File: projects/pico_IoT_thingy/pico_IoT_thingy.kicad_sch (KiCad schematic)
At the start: 2 parts, among them U1 TSR1-2450E

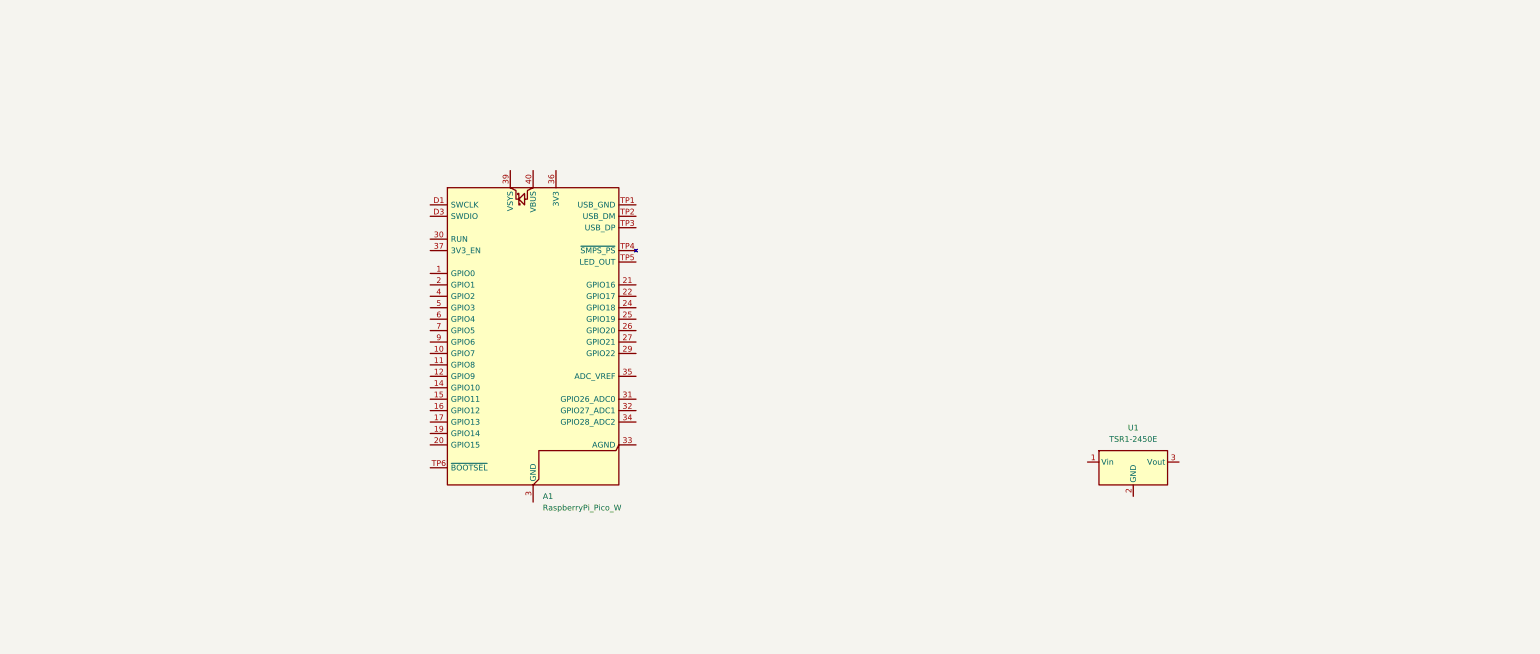
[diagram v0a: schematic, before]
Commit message: Pico IoT thingy - Add 5V to 3V3 bar
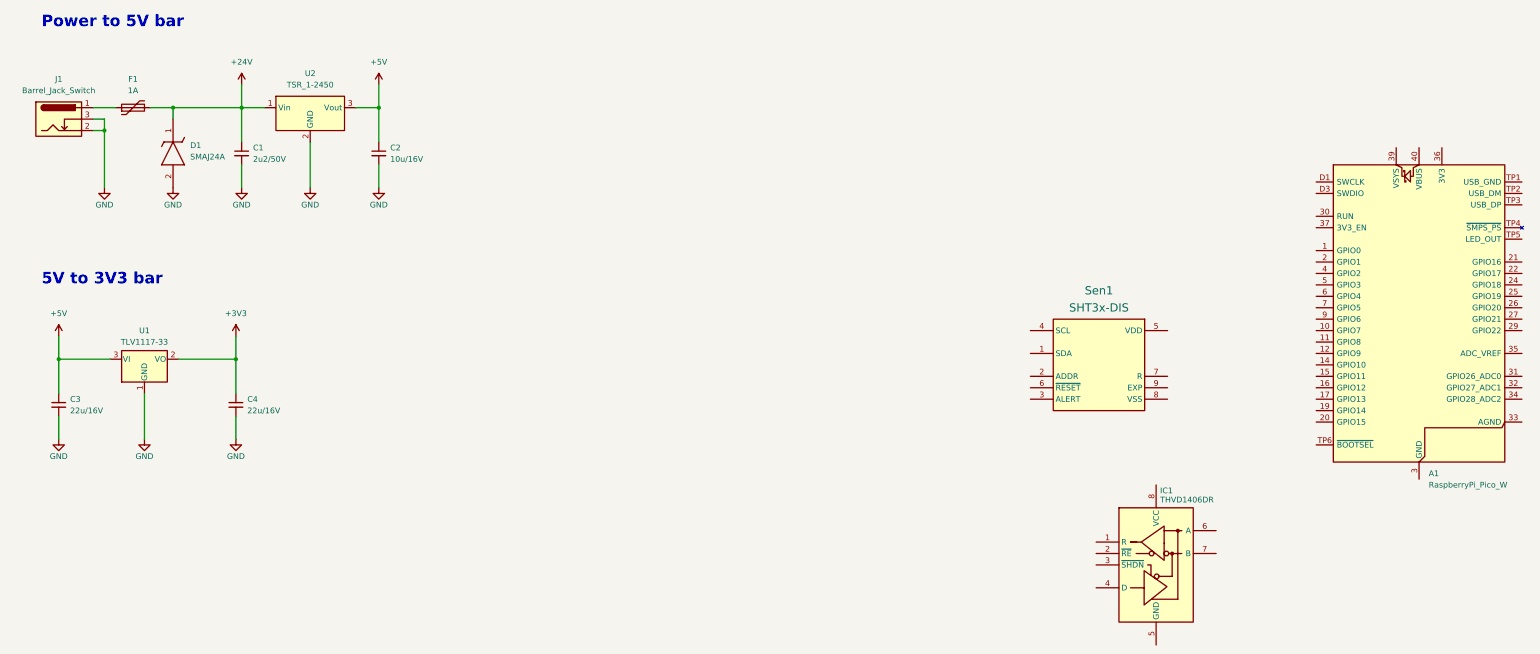
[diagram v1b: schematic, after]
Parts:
- removed U1: TSR1-2450E, Converter_DCDC:Converter_DCDC_TRACO_TSR1-xxxxE_THT, symbol Converter_DCDC:TSR1-2450E
- added C1: 2u2/50V, symbol Device:C_Small
- added C2: 10u/16V, symbol Device:C_Small
- added C3, C4: 22u/16V, symbol Device:C_Small
- added D1: SMAJ24A, DIOM5127X229N, symbol MH_SMAJ24A:SMAJ24A
- added F1: 1A, symbol Device:Polyfuse
- added IC1: THVD1406DR, SOIC127P600X175-8N, symbol MH_THVD1406DR:THVD1406DR
- added J1: Barrel_Jack_Switch, symbol Connector:Barrel_Jack_Switch
- added Sen1: SHT3x-DIS, symbol MH_SHT31-DIS:SHT3x-DIS
- added U1: TLV1117-33, symbol Regulator_Linear:TLV1117-33
- added U2: TSR_1-2450, Converter_DCDC:Converter_DCDC_TRACO_TSR-1_THT, symbol Converter_DCDC:TSR_1-2450
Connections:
- new net: F1.1, J1.1
- new net +24V: C1.1, D1.1 (K), F1.2, U2.1 (Vin)
- new net +3V3: C4.1, U1.2 (VO)
- new net +5V: C2.1, C3.1, U1.3 (VI), U2.3 (Vout)
- new net GND: C1.2, C2.2, C3.2, C4.2, D1.2 (A), J1.2, J1.3, U1.1 (GND), U2.2 (GND)
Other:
- note added: "5V to 3V3 bar"
- note added: "Power to 5V bar"
- moved on the sheet: A1

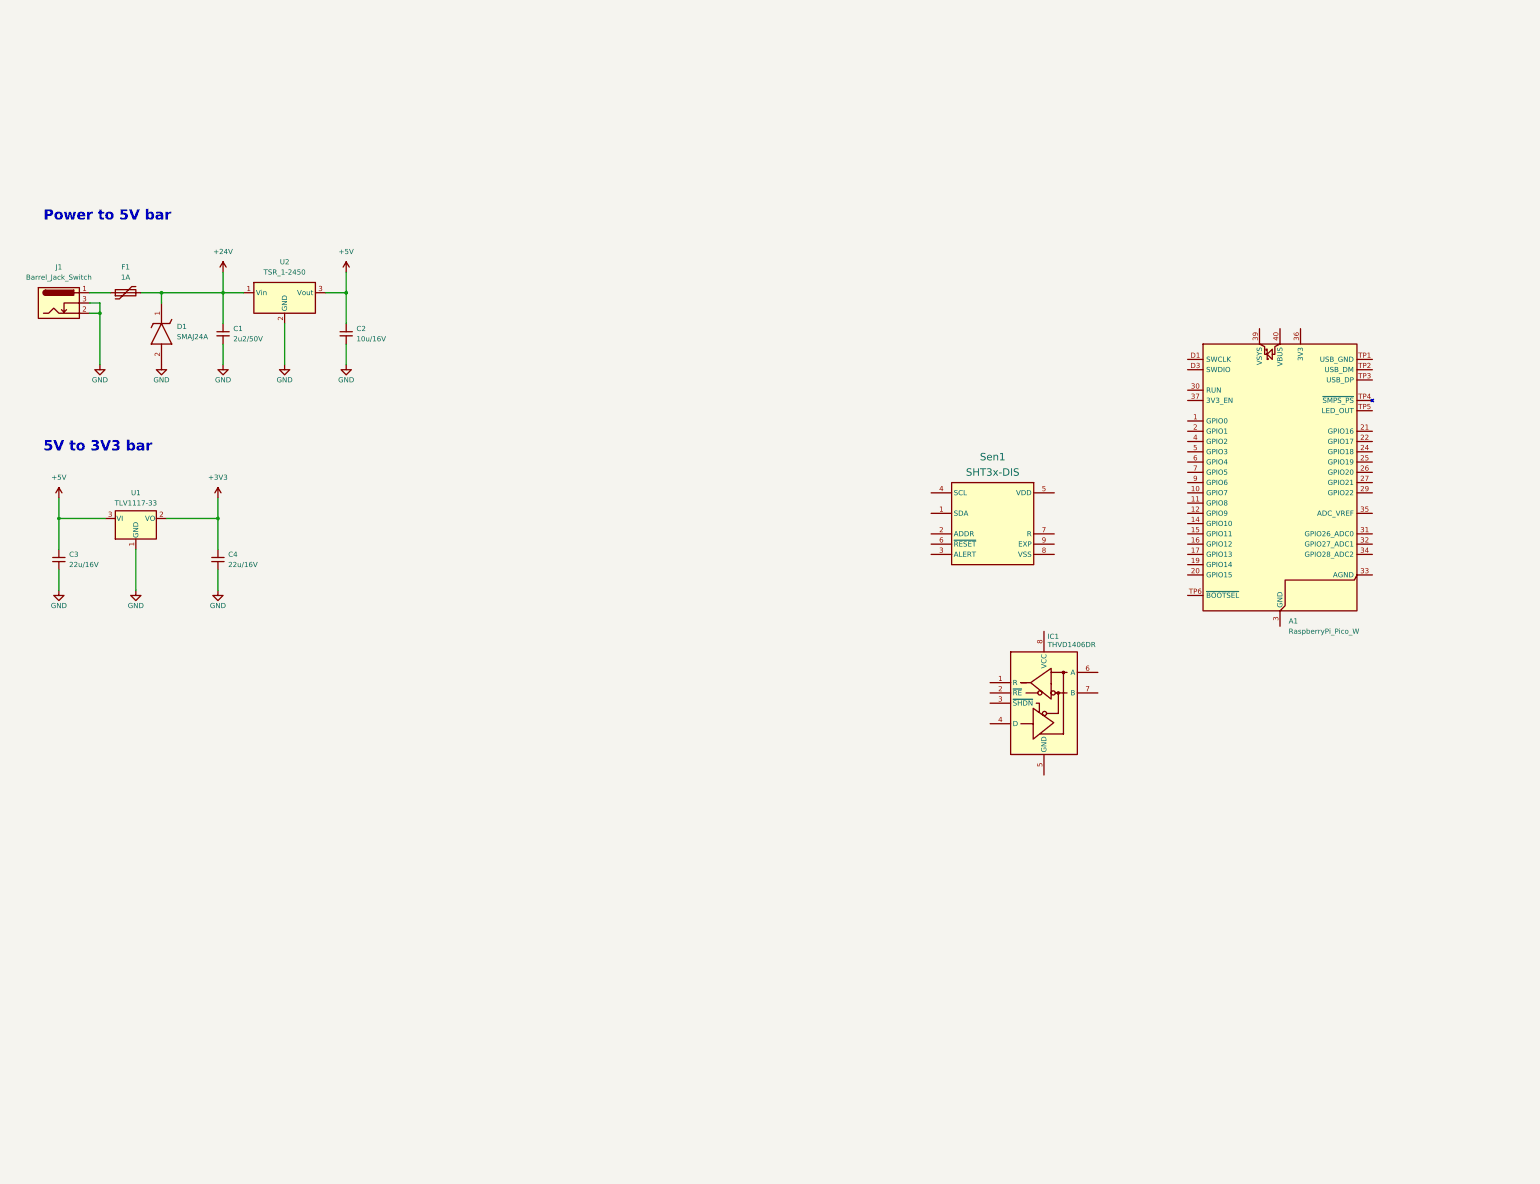
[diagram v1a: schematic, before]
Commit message: Pico IoT thingy - progress on schematics
- user-programmable button
- RGB LED
- DIP switch to set address
- SPI port
- SHT31 sensor
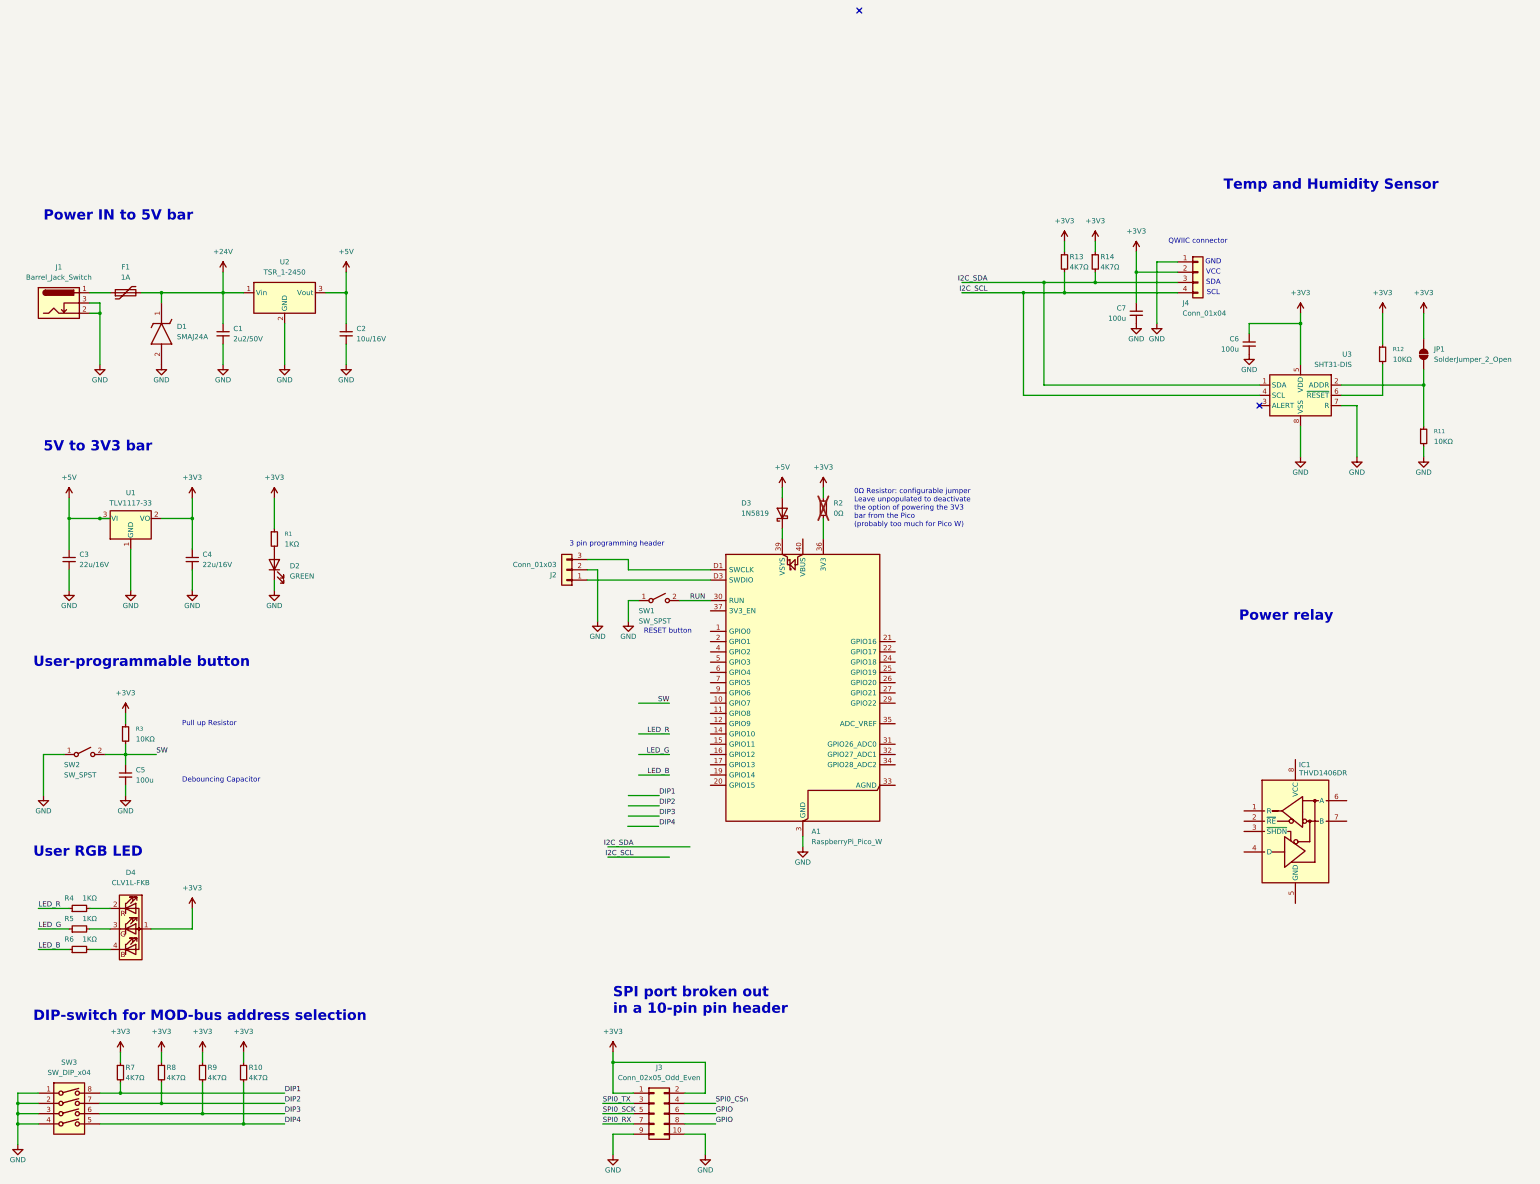
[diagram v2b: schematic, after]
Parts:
- removed A1: RaspberryPi_Pico_W, Module:RaspberryPi_Pico_W_SMD, symbol MCU_Module:RaspberryPi_Pico_W_Extensive
- removed Sen1: SHT3x-DIS, symbol MH_SHT31-DIS:SHT3x-DIS
- added A1: RaspberryPi_Pico_W, Module:RaspberryPi_Pico_W_SMD_HandSolder, symbol MCU_Module:RaspberryPi_Pico_W_Debug
- added C5, C6, C7: 100u, symbol Device:C_Small
- added D2: GREEN, symbol Device:LED
- added D3: 1N5819, Diode_THT:D_DO-41_SOD81_P10.16mm_Horizontal, symbol Diode:1N5819
- added D4: CLV1L-FKB, LED_SMD:LED_Cree-PLCC4_3.2x2.8mm_CCW, symbol LED:CLV1L-FKB
- added J2: Conn_01x03, symbol Connector_Generic:Conn_01x03
- added J3: Conn_02x05_Odd_Even, symbol Connector_Generic:Conn_02x05_Odd_Even
- added J4: Conn_01x04, symbol Connector_Generic:Conn_01x04
- added JP1: SolderJumper_2_Open, symbol Jumper:SolderJumper_2_Open
- added R1, R4, R5, R6: 1KΩ, symbol Device:R_Small
- added R10, R13, R14, R7, R8, R9: 4K7Ω, symbol Device:R_Small
- added R11, R12, R3: 10KΩ, symbol Device:R_Small
- added R2: 0Ω, symbol Device:R_Small
- added SW1, SW2: SW_SPST, symbol Switch:SW_SPST
- added SW3: SW_DIP_x04, symbol Switch:SW_DIP_x04
- added U3: SHT31-DIS, Sensor_Humidity:Sensirion_DFN-8-1EP_2.5x2.5mm_P0.5mm_EP1.1x1.7mm, symbol Sensor_Humidity:SHT31-DIS
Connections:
- net +3V3: now also C6.1, C7.1, D4.1 (A), J3.1 (Pin_1), J3.2 (Pin_2), J4.2 (Pin_2), JP1.2 (B), R1.1, R10.1, R12.1, R13.1, R14.1, R2.1, R3.1, R7.1, R8.1, R9.1, U3.5 (VDD)
- net +5V: now also D3.2 (A)
- net GND: now also A1.13 (GND), A1.18 (GND), A1.23 (GND), A1.28 (GND), A1.3 (GND), A1.38 (GND), A1.8 (GND), A1.D2 (GND), C5.2, C6.2, C7.2, D2.1 (K), J2.2 (Pin_2), J3.10 (Pin_10), J3.9 (Pin_9), J4.1 (Pin_1), R11.2, SW1.1 (A), SW2.1 (A), SW3.1, SW3.2, SW3.3, SW3.4, U3.7 (R), U3.8 (VSS), U3.9 (VSS)
- new net: R12.2, U3.6 (~{RESET})
- new net: A1.D3 (SWDIO), J2.1 (Pin_1)
- new net: A1.D1 (SWCLK), J2.3 (Pin_3)
- new net: A1.36 (3V3), R2.2
- new net: A1.39 (VSYS), D3.1 (K)
- new net: D4.2 (RK), R4.2
- new net: D4.3 (GK), R5.2
- new net: D4.4 (BK), R6.2
- new net: JP1.1 (A), R11.1, U3.2 (ADDR)
- new net: D2.2 (A), R1.2
- new net DIP1: R7.2, SW3.8
- new net DIP2: R8.2, SW3.7
- new net DIP3: R9.2, SW3.6
- new net DIP4: R10.2, SW3.5
- new net GPIO: J3.6 (Pin_6), J3.8 (Pin_8)
- new net I2C_SCL: J4.4 (Pin_4), R13.2, U3.4 (SCL)
- new net I2C_SDA: J4.3 (Pin_3), R14.2, U3.1 (SDA)
- new net LED_B: R6.1
- new net LED_G: R5.1
- new net LED_R: R4.1
- new net RUN: A1.30 (RUN), SW1.2 (B)
- new net SPI0_CSn: J3.4 (Pin_4)
- new net SPI0_RX: J3.7 (Pin_7)
- new net SPI0_SCK: J3.5 (Pin_5)
- new net SPI0_TX: J3.3 (Pin_3)
- new net SW: C5.1, R3.2, SW2.2 (B)
- no-connect marks 0 -> 2
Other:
- note added: "0Ω Resistor: configurable jumper Leave unpopulated to deactivate the option of powering the 3V3 bar from the Pico (probably too much for Pico W)"
- note added: "3 pin programming header"
- note added: "DIP-switch for MOD-bus address selection"
- note added: "Debouncing Capacitor"
- note added: "GND"
- note added: "Power IN to 5V bar"
- note added: "Power relay"
- note added: "Pull up Resistor"
- note added: "QWIIC connector"
- note added: "RESET button"
- note added: "SCL"
- note added: "SDA"
- note added: "SPI port broken out in a 10-pin pin header"
- note added: "Temp and Humidity Sensor"
- note added: "User RGB LED"
- note added: "User-programmable button"
- note added: "VCC"
- note removed: "Power to 5V bar"
- moved on the sheet: C3, C4, IC1, U1

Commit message: Pico IoT thingy - complete schematics, DRC OK
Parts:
- removed D3: 1N5819, Diode_THT:D_DO-41_SOD81_P10.16mm_Horizontal, symbol Diode:1N5819
- added C8: 100n, symbol Device:C_Small
- added D3: SM712_SOT23, Package_TO_SOT_SMD:SOT-23, symbol Diode:SM712_SOT23
- added D5: YELLOW, symbol Device:LED
- added D6, D7: SS14, Diode_SMD:D_SMA, symbol Diode:SS14
- added H1, H2, H3, H4: MountingHole_Pad, symbol Mechanical:MountingHole_Pad
- added J5: Screw_Terminal_01x03, symbol Connector:Screw_Terminal_01x03
- added J6: Screw_Terminal_01x04, symbol Connector:Screw_Terminal_01x04
- added J7: Conn_01x02, symbol Connector_Generic:Conn_01x02
- added K1: RT314A05, Relay_THT:Relay_SPDT_Schrack-RT1-16A-FormC_RM5mm, symbol Relay:RT314A05
- added Q1: BC817, Package_TO_SOT_SMD:SOT-23, symbol Transistor_BJT:BC817
- added R15, R17: 1KΩ, symbol Device:R_Small
- added R16: 10KΩ, symbol Device:R_Small
- added R18, R19: 10Ω, symbol Device:R_Small
- added R20: 120Ω, symbol Device:R_Small
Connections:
- net I2C_SCL is gone; now on net I2C1_SCL: J4.4 (Pin_4), R13.2, U3.4 (SCL)
- net I2C_SDA is gone; now on net I2C1_SDA: J4.3 (Pin_3), R14.2, U3.1 (SDA)
- net +3V3: now also IC1.2 (~{RE}), IC1.3 (~{SHDN}), IC1.8 (VCC), C8.1
- net +5V: now also D6.1 (K), D7.2 (A), J6.3 (Pin_3), K1.A1, R15.1
- net DIP1: now also A1.29 (GPIO22)
- net DIP2: now also A1.27 (GPIO21)
- net DIP3: now also A1.26 (GPIO20)
- net DIP4: now also A1.25 (GPIO19)
- net GND: now also IC1.5 (GND), C8.2, D3.3 (common), H1.1, H2.1, H3.1, H4.1, J6.4 (Pin_4), Q1.2 (E), R16.2
- net LED_B: now also A1.21 (GPIO16)
- net LED_G: now also A1.22 (GPIO17)
- net LED_R: now also A1.24 (GPIO18)
- net SPI0_CSn: now also A1.7 (GPIO5)
- net SPI0_RX: now also A1.6 (GPIO4)
- net SPI0_SCK: now also A1.4 (GPIO2)
- net SPI0_TX: now also A1.5 (GPIO3)
- net SW: now also A1.17 (GPIO13)
- net UART0_TX: now reaches A1.1 (GPIO0)
- net UART0_TX: now also IC1.4 (D)
- net I2C1_SCL: now reaches A1.10 (GPIO7)
- net RELAY: now reaches A1.15 (GPIO11)
- net RELAY: now also R17.1
- net UART0_RX: now reaches A1.2 (GPIO1)
- net UART0_RX: now also IC1.1 (R)
- net GPIO26: now reaches A1.31 (GPIO26_ADC0)
- net GPIO26: now also J3.6 (Pin_6)
- net GPIO27: now reaches A1.32 (GPIO27_ADC1)
- net GPIO27: now also J3.8 (Pin_8)
- net at A1.39 (VSYS): now also D7.1 (K)
- net I2C1_SDA: now reaches A1.9 (GPIO6)
- net at IC1.6 (A): now also D3.2 (A2), J7.2 (Pin_2), R19.1
- net at IC1.7 (B): now also D3.1 (A1), R18.1, R20.2
- removed net GPIO: J3.6 (Pin_6), J3.8 (Pin_8)
- new net: Q1.1 (B), R16.1, R17.2
- new net: D5.1 (K), D6.2 (A), K1.A2, Q1.3 (C)
- new net: J5.2 (Pin_2), K1.11
- new net: J5.1 (Pin_1), K1.12
- new net: J5.3 (Pin_3), K1.14
- new net: D5.2 (A), R15.2
- new net: J7.1 (Pin_1), R20.1
- new net A: J6.2 (Pin_2), R19.2
- new net B: J6.1 (Pin_1), R18.2
- no-connect marks 2 -> 12
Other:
- note added: "3-pin programming header"
- note added: "DC-DC 24V Power IN to 5V bar"
- note added: "DIP switch"
- note added: "Decoupling Capacitor"
- note added: "Diode in reverse to protect the MCU from relay spikes"
- note added: "Extra GPIO pins for the SPI port"
- note added: "Green LED indicates power ON"
- note added: "I/O Pins SPI port broken out in a 10-pin header"
- note added: "I2C"
- note added: "I2C Temp and Humidity Sensor + QWIIC Connector"
- note added: "LDO 5V to 3V3 bar"
- note added: "Mounting Holes"
- note added: "Not seen in documentation..."
- note added: "RS485 connector"
- note added: "Raspberry Pi Pico (W)"
- note added: "Relay"
- note added: "SPI"
- note added: "Transient protection"
- note added: "UART"
- note added: "User I/O RGB LED"
- note added: "Yellow LED indicates that the relay is ON"
- note added: "pull-down resistor"
- note removed: "3 pin programming header"
- note removed: "5V to 3V3 bar"
- note removed: "Power IN to 5V bar"
- note removed: "SPI port broken out in a 10-pin pin header"
- note removed: "Temp and Humidity Sensor"
- moved on the sheet: A1, C1, C2, C3, C4, C5, D1, D2, D4, F1, IC1, J1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

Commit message: Pico IoT thingy - visual cleanup of schematics
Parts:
- renumbered C6 to C1, C1 to C2, C2 to C3, C7 to C4, C3 to C5, C4 to C6, C5 to C7, D7 to D2, D2 to D3, D6 to D4, D4 to D6, D3 to D7, J4 to J2, J2 to J3, J5 to J4, J6 to J5, J3 to J6, R12 to R1, R16 to R10, R4 to R11, R5 to R12, R6 to R13, R20 to R14, R18 to R15, R19 to R16, R7 to R17, R8 to R18, R9 to R19, R11 to R2, R10 to R20, R13 to R3, R14 to R4, R2 to R5, R1 to R6, R15 to R7, R3 to R8, R17 to R9, U2 to U1, U3 to U2, U1 to U3
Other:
- note added: "?"
- note added: "Diode in reverse to protect the circuit from spikes in relay"
- note removed: "Diode in reverse to protect the MCU from relay spikes"
- moved on the sheet: A1, C1, C2, C3, C4, C5, C6, C7, C8, D1, D2, D3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
